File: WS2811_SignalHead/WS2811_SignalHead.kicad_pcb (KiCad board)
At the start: 2 copper layers, 33 x 37.7 mm, 17 parts, among them K1 +5 In GND, K2 +5 Out GND, P1 C Y G R, P2 C, P3 R, P4 Y, P5 G, U1 WS2811

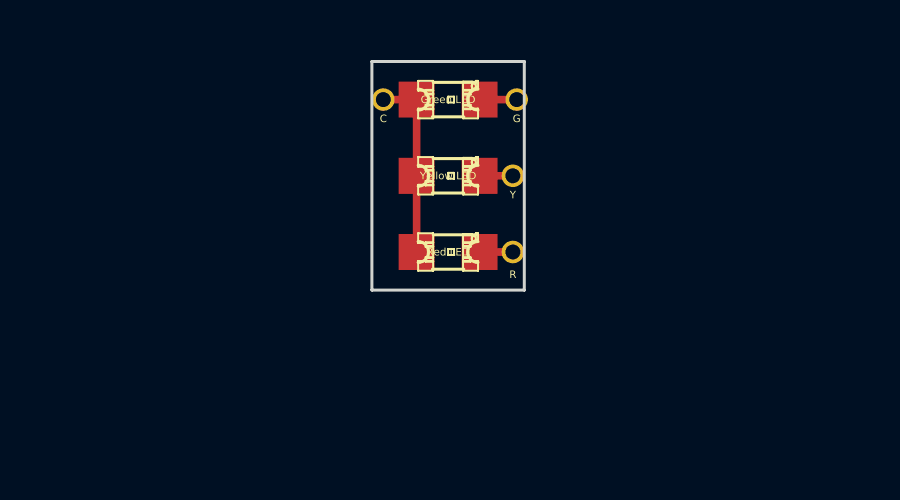
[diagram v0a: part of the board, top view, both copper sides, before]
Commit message: Minor updates to WS2811_SignalHead: adjust terminal points on the signal head board.
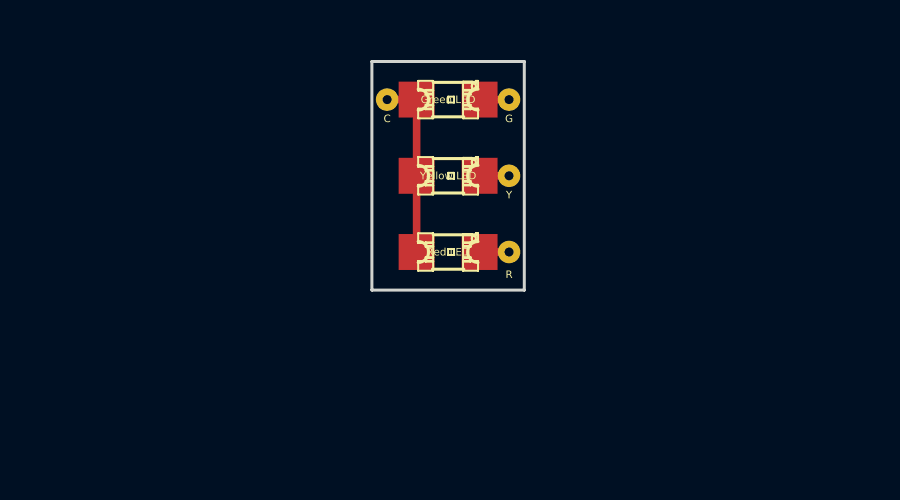
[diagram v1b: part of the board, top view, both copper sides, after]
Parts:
- moved P5 0.25 mm to (192.5, 88.0)
- moved P2 0.13 mm to (188.5, 88.0)
- moved P3 0.13 mm to (192.5, 93.1)
- moved P4 0.13 mm to (192.5, 90.6)
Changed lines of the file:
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@@
     (mod_text_width 0.15)
     (pad_size 0.75 0.75)
-    (pad_drill 0.5)
+    (pad_drill 0.3)
     (pad_to_mask_clearance 0)
     (aux_axis_origin 0 0)
@@
   )
   (module microterm (layer F.Cu)
-    (at 192.659 93.091)
+    (at 192.532 93.091)
     (fp_text reference P3 (at 0 0) (layer F.SilkS) hide
       (effects (font (size 1 1) (thickness 0.15)))
@@
       (effects (font (size 0.25 0.25) (thickness 0.03)))
     )
-    (pad 1 thru_hole circle (at 0 0) (size 0.75 0.75) (drill 0.5)
+    (pad 1 thru_hole circle (at 0 0) (size 0.75 0.75) (drill 0.3)
       (layers *.Cu *.Mask F.SilkS)
       (net 13 Red)
@@
   )
   (module microterm (layer F.Cu)
-    (at 192.659 90.551)
+    (at 192.532 90.551)
     (fp_text reference P4 (at 0 0) (layer F.SilkS) hide
       (effects (font (size 1 1) (thickness 0.15)))
@@
       (effects (font (size 0.25 0.25) (thickness 0.03)))
     )
-    (pad 1 thru_hole circle (at 0 0) (size 0.75 0.75) (drill 0.5)
+    (pad 1 thru_hole circle (at 0 0) (size 0.75 0.75) (drill 0.3)
       (layers *.Cu *.Mask F.SilkS)
       (net 14 Yellow)
@@
   )
   (module microterm (layer F.Cu)
-    (at 192.786 88.011)
+    (at 192.532 88.011)
     (fp_text reference P5 (at 0 0) (layer F.SilkS) hide
       (effects (font (size 1 1) (thickness 0.15)))
@@
       (effects (font (size 0.25 0.25) (thickness 0.03)))
     )
-    (pad 1 thru_hole circle (at 0 0) (size 0.75 0.75) (drill 0.5)
+    (pad 1 thru_hole circle (at 0 0) (size 0.75 0.75) (drill 0.3)
       (layers *.Cu *.Mask F.SilkS)
       (net 4 Green)
@@
   )
   (module microterm (layer F.Cu)
-    (at 188.341 88.011)
+    (at 188.468 88.011)
     (fp_text reference P2 (at 0 0) (layer F.SilkS) hide
       (effects (font (size 1 1) (thickness 0.15)))
@@
       (effects (font (size 0.25 0.25) (thickness 0.03)))
     )
-    (pad 1 thru_hole circle (at 0 0) (size 0.75 0.75) (drill 0.5)
+    (pad 1 thru_hole circle (at 0 0) (size 0.75 0.75) (drill 0.3)
       (layers *.Cu *.Mask F.SilkS)
       (net 2 "Common (+)")
@@
   (segment (start 200.533 113.03) (end 200.66 113.157) (width 0.254) (layer B.Cu) (net 1))
   (via (at 200.533 113.03) (size 0.889) (layers F.Cu B.Cu) (net 1))
-  (segment (start 189.45098 88.011) (end 188.341 88.011) (width 0.254) (layer F.Cu) (net 2) (status C00000))
+  (segment (start 189.45098 88.011) (end 188.468 88.011) (width 0.254) (layer F.Cu) (net 2))
   (segment (start 189.45098 93.091) (end 189.45098 90.551) (width 0.254) (layer F.Cu) (net 2))
   (segment (start 189.45098 88.011) (end 189.45098 90.551) (width 0.254) (layer F.Cu) (net 2))
@@
   (segment (start 203.073 110.871) (end 188.341 110.871) (width 0.254) (layer F.Cu) (net 3))
   (segment (start 203.454 110.49) (end 203.073 110.871) (width 0.254) (layer F.Cu) (net 3))
-  (segment (start 191.54902 88.011) (end 192.786 88.011) (width 0.254) (layer F.Cu) (net 4))
+  (segment (start 191.54902 88.011) (end 192.532 88.011) (width 0.254) (layer F.Cu) (net 4))
   (segment (start 198.12 115.57) (end 195.58 115.57) (width 0.254) (layer F.Cu) (net 5))
   (segment (start 195.58 115.57) (end 194.31 116.84) (width 0.254) (layer F.Cu) (net 5))
@@
   (via (at 188.595 119.507) (size 0.889) (layers F.Cu B.Cu) (net 12))
   (segment (start 188.722 119.38) (end 188.595 119.507) (width 0.254) (layer F.Cu) (net 12))
-  (segment (start 191.54902 93.091) (end 192.659 93.091) (width 0.254) (layer F.Cu) (net 13))
-  (segment (start 191.54902 90.551) (end 192.659 90.551) (width 0.254) (layer F.Cu) (net 14))
+  (segment (start 192.532 93.091) (end 191.54902 93.091) (width 0.254) (layer F.Cu) (net 13))
+  (segment (start 192.532 90.551) (end 191.54902 90.551) (width 0.254) (layer F.Cu) (net 14))
 )

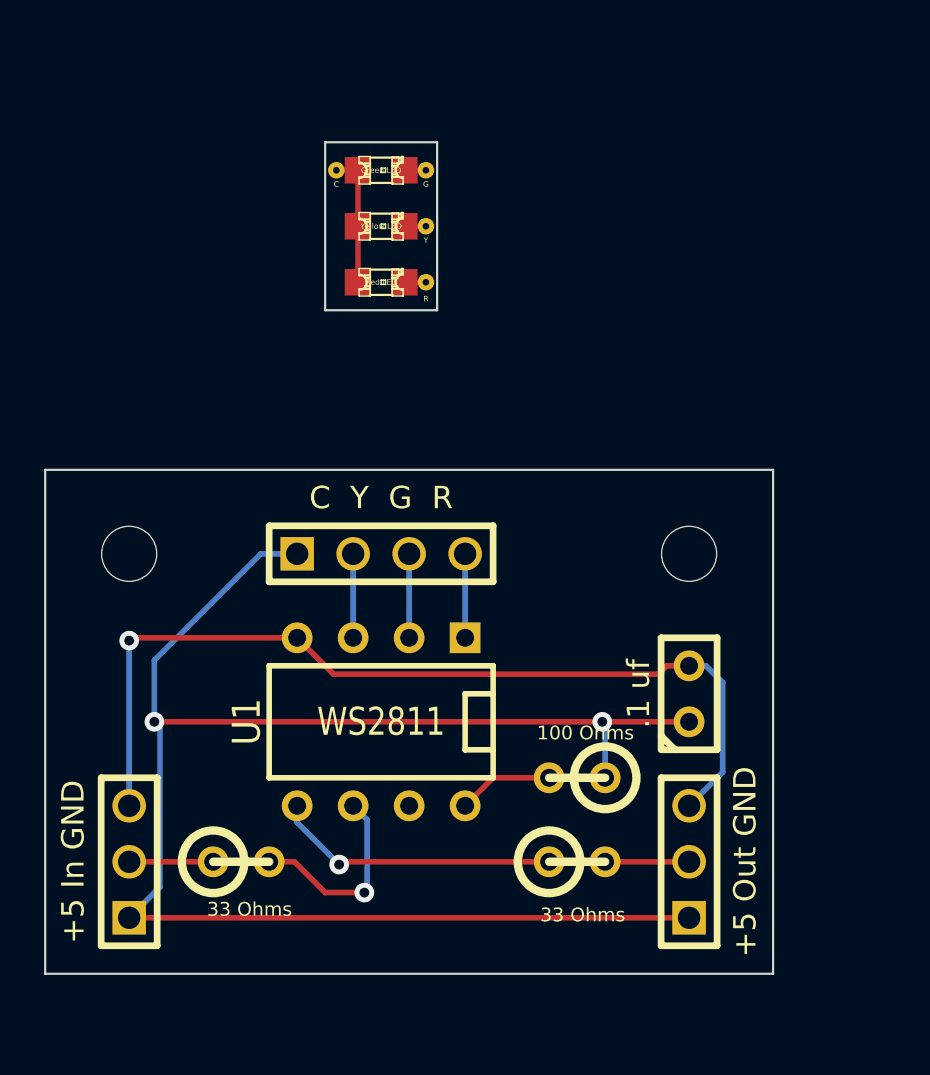
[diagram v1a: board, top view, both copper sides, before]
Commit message: Updated WS2811_SignalHead: Signal Head board matches Oregon Rail signal heads.  Updated driver board to be 25.4 mm x 31.8 mm, using 3.7mm mounting holes.
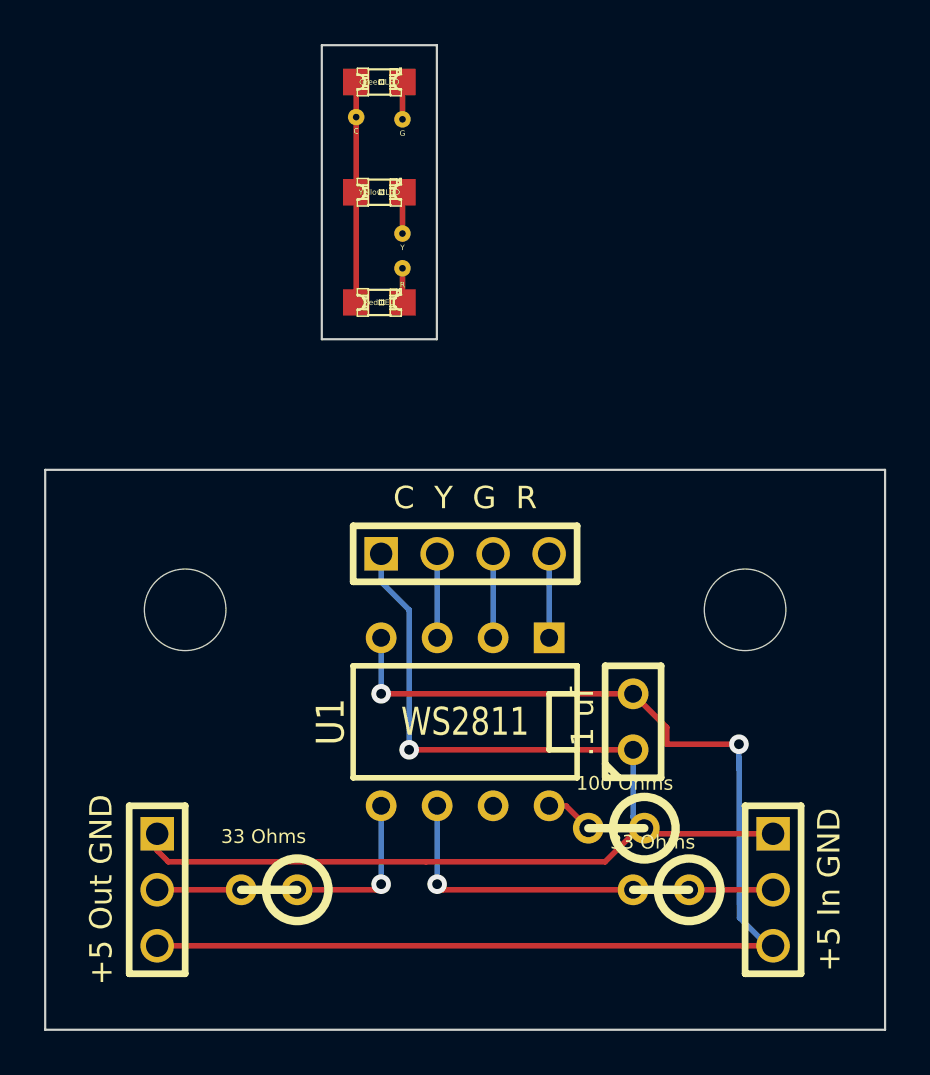
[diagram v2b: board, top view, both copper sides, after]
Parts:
- removed the MH at (179.1, 105.4)
- removed the MH at (204.5, 105.4)
- added MH: MountingHole_3-7mm_RevA_Date21Jun2010, MountingHole_3-7mm_RevA_Date21Jun2010, F.Cu at (181.6, 108.0)
- added MH: MountingHole_3-7mm_RevA_Date21Jun2010, MountingHole_3-7mm_RevA_Date21Jun2010, F.Cu at (207.0, 108.0)
- moved K1 29.2 mm to (208.3, 120.7), turned to 270 degrees
- moved K2 24.2 mm to (180.3, 120.7), turned to 270 degrees
- moved R1 19.1 mm to (203.2, 120.7), turned to 180 degrees
- moved R3 14.0 mm to (185.4, 120.7), turned to 180 degrees
- moved D3 4.01 mm to (190.4, 84.0)
- moved P1 3.81 mm to (194.3, 105.4)
- moved U1 3.81 mm to (194.3, 113.0)
- moved R2 2.90 mm to (201.2, 117.9)
- moved C1 2.84 mm to (201.9, 113.0)
- moved P2 2.58 mm to (189.4, 85.6)
- moved P5 2.54 mm to (191.5, 85.7)
- moved D2 1.55 mm to (190.4, 89.0)
- moved P3 1.24 mm to (191.5, 92.5)
- moved P4 1.12 mm to (191.5, 90.9)
- moved D1 0.92 mm to (190.4, 94.0)
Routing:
- net +5V: track 73.1 -> 53.8 mm, vias 2 -> 1
- net GND: track 41.8 -> 58.1 mm, vias 1 -> 2
- net N-000006: track 13.0 -> 7.47 mm
- net Common (+): track 6.06 -> 10.0 mm
- net N-000003: track 9.15 -> 12.6 mm
- net N-0000011: track 4.34 -> 2.20 mm
- net Yellow: track 0.98 -> 1.87 mm
- net Green: track 0.98 -> 1.69 mm
- net Red: track 0.98 -> 1.55 mm
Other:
- board size 33 x 37.7 mm -> 38.1 x 44.7 mm
